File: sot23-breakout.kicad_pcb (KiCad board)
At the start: 2 copper layers, 15.2 x 10.2 mm, 6 parts, among them J1 Conn_01x06, J2 Conn_01x06, Q1 Q_NMOS_GSD, Q2 Q_NMOS_GSD, Q3 Q_NMOS_GSD, Q4 Q_NMOS_GSD

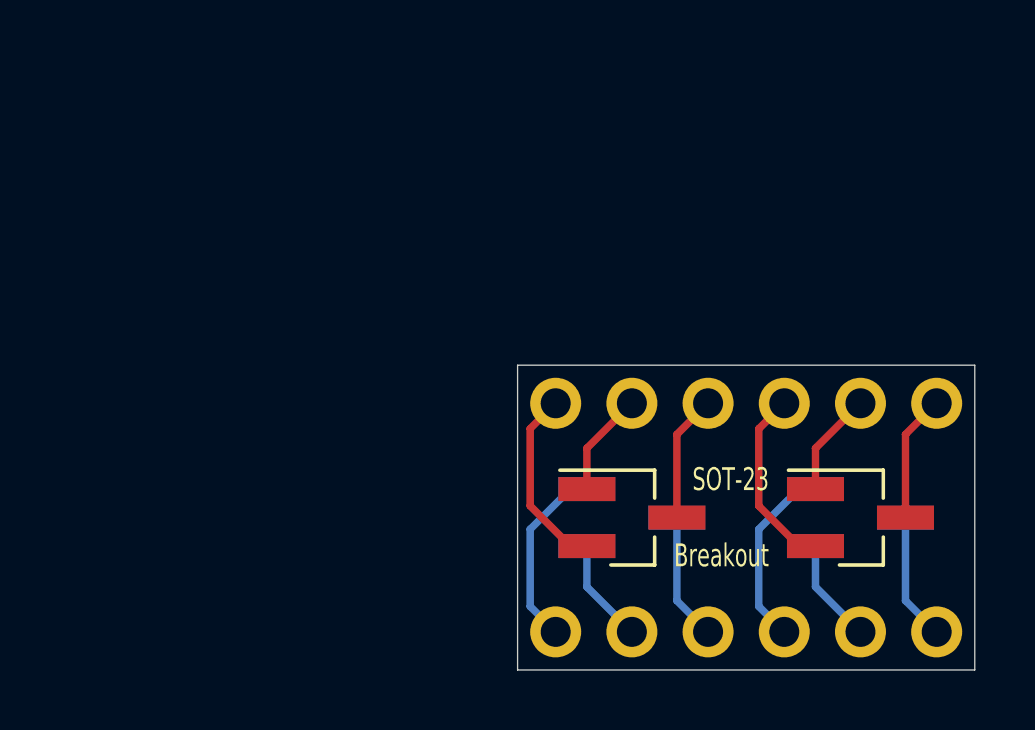
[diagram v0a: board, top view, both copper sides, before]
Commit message: change SOT-23 breakout to have 8 chips
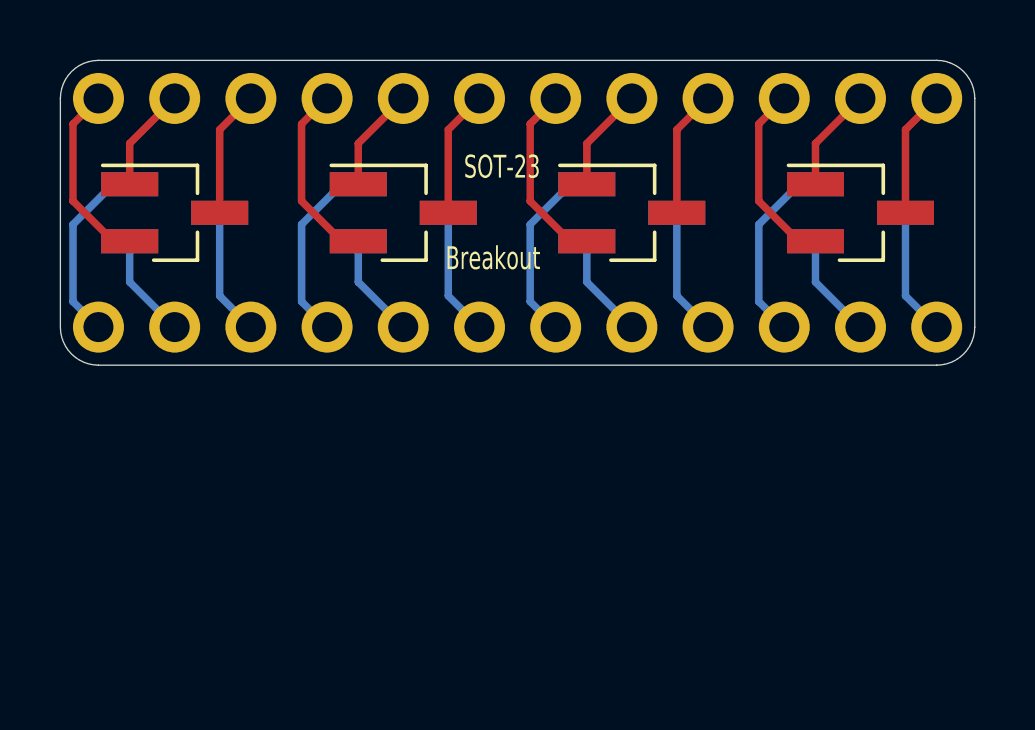
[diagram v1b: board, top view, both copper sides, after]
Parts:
- added Q5: Q_NMOS_GSD, Package_TO_SOT_SMD:SOT-23_Handsoldering, B.Cu at (129.5, 80.0)
- added Q6: Q_NMOS_GSD, Package_TO_SOT_SMD:SOT-23_Handsoldering, B.Cu at (137.2, 80.0)
- added Q7: Q_NMOS_GSD, Package_TO_SOT_SMD:SOT-23_Handsoldering, B.Cu at (144.8, 80.0)
- added Q8: Q_NMOS_GSD, Package_TO_SOT_SMD:SOT-23_Handsoldering, B.Cu at (152.4, 80.0)
- J1, J2: value Conn_01x06 -> Conn_01x12; footprint footprints:Header_1x06_P2.54mm -> footprints:Header_1x12_P2.54mm
- Q1, Q2: moved to F.Cu
- moved Q4 25.0 mm to (129.5, 80.0)
- moved J1 23.4 mm to (127.0, 76.2)
- moved J2 15.5 mm to (127.0, 83.8)
- moved Q3 12.7 mm to (137.2, 80.0)
- moved Q1 10.2 mm to (152.4, 80.0)
- moved Q2 10.2 mm to (144.8, 80.0)
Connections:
- Q1 pad 1: Net-(J1-Pad5) -> Net-(J1-Pad11)
- Q1 pad 2: Net-(J1-Pad4) -> Net-(J1-Pad10)
- Q1 pad 3: Net-(J1-Pad6) -> Net-(J1-Pad12)
- Q2 pad 1: Net-(J1-Pad2) -> Net-(J1-Pad8)
- Q2 pad 2: Net-(J1-Pad1) -> Net-(J1-Pad7)
- Q2 pad 3: Net-(J1-Pad3) -> Net-(J1-Pad9)
- Q3 pad 1: Net-(J2-Pad2) -> Net-(J1-Pad5)
- Q3 pad 2: Net-(J2-Pad1) -> Net-(J1-Pad4)
- Q3 pad 3: Net-(J2-Pad3) -> Net-(J1-Pad6)
- Q4 pad 1: Net-(J2-Pad5) -> Net-(J1-Pad2)
- Q4 pad 2: Net-(J2-Pad4) -> Net-(J1-Pad1)
- Q4 pad 3: Net-(J2-Pad6) -> Net-(J1-Pad3)
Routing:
- net Net-(J2-Pad10): track 0.00 -> 6.22 mm
- net Net-(J1-Pad10): track 0.00 -> 6.22 mm
- net Net-(J2-Pad7): track 0.00 -> 6.22 mm
- net Net-(J1-Pad7): track 0.00 -> 6.22 mm
- net Net-(J1-Pad9): track 0.00 -> 4.24 mm
- net Net-(J1-Pad12): track 0.00 -> 4.24 mm
- net Net-(J2-Pad9): track 0.00 -> 4.24 mm
- net Net-(J2-Pad12): track 0.00 -> 4.24 mm
- net Net-(J2-Pad8): track 0.00 -> 3.48 mm
- net Net-(J2-Pad11): track 0.00 -> 3.48 mm
- net Net-(J1-Pad8): track 0.00 -> 3.48 mm
- net Net-(J1-Pad11): track 0.00 -> 3.48 mm
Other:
- board size 15.2 x 10.2 mm -> 30.5 x 10.2 mm
